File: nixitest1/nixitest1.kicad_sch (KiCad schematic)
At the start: 32 parts, among them J1 MSYS, Q1 60V 3A, Q10 HVN, Q11 HVN, Q12 HVN, Q13 HVN, Q2 HVN, Q3 HVN, Q4 HVN, Q5 HVN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

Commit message: Update schematic and design.
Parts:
- added J5, J6: ~, rawpad22:rawpad22, symbol Connector_Generic:Conn_01x01
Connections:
- net PGM: now also J5.1 (Pin_1); no longer J4.1 (Pin_1)
- net URX: now also J4.1 (Pin_1)
- net UTX: now also J6.1 (Pin_1)
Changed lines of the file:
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@@
+    )
+  )
+  (global_label "UTX" (shape input) (at 132.08 177.8 270) (fields_autoplaced)
+    (effects (font (size 1.27 1.27)) (justify right))
+    (property "Intersheet References" "${INTERSHEET_REFS}" (id 0) (at 132.0006 183.7207 90)
+      (effects (font (size 1.27 1.27)) (justify right) hide)
     )
   )
@@
     )
   )
-  (global_label "PGM" (shape input) (at 166.37 165.1 270) (fields_autoplaced)
-    (effects (font (size 1.27 1.27)) (justify right))
-    (property "Intersheet References" "${INTERSHEET_REFS}" (id 0) (at 166.4494 171.5045 90)
+  (global_label "PGM" (shape input) (at 129.54 177.8 270) (fields_autoplaced)
+    (effects (font (size 1.27 1.27)) (justify right))
+    (property "Intersheet References" "${INTERSHEET_REFS}" (id 0) (at 129.6194 184.2045 90)
+      (effects (font (size 1.27 1.27)) (justify right) hide)
+    )
+  )
+  (global_label "URX" (shape input) (at 124.46 177.8 270) (fields_autoplaced)
+    (effects (font (size 1.27 1.27)) (justify right))
+    (property "Intersheet References" "${INTERSHEET_REFS}" (id 0) (at 124.3806 184.0231 90)
       (effects (font (size 1.27 1.27)) (justify right) hide)
     )
@@
     )
   )
+  (symbol (lib_id "Connector_Generic:Conn_01x01") (at 132.08 172.72 90) (unit 1)
+    (in_bom yes) (on_board yes)
+    (property "Reference" "J6" (id 0) (at 134.62 171.4499 90)
+      (effects (font (size 1.27 1.27)) (justify right) hide)
+    )
+    (property "Value" "~" (id 1) (at 116.84 173.9899 90)
+      (effects (font (size 1.27 1.27)) (justify right))
+    )
+    (property "Footprint" "rawpad22:rawpad22" (id 2) (at 132.08 172.72 0)
+      (effects (font (size 1.27 1.27)) hide)
+    )
+    (property "Datasheet" "~" (id 3) (at 132.08 172.72 0)
+      (effects (font (size 1.27 1.27)) hide)
+    )
+    (pin "1")
+  )
   (symbol (lib_id "power:GND") (at 256.54 114.3 0) (unit 1)
     (in_bom yes) (on_board yes) (fields_autoplaced)
@@
     (pin "1")
   )
-  (symbol (lib_id "Connector_Generic:Conn_01x01") (at 161.29 160.02 90) (unit 1)
-    (in_bom yes) (on_board yes) (fields_autoplaced)
-    (property "Reference" "J2" (id 0) (at 163.83 158.7499 90)
-      (effects (font (size 1.27 1.27)) (justify right) hide)
-    )
-    (property "Value" "~" (id 1) (at 163.83 161.2899 90)
+  (symbol (lib_id "Connector_Generic:Conn_01x01") (at 121.92 172.72 90) (unit 1)
+    (in_bom yes) (on_board yes)
+    (property "Reference" "J2" (id 0) (at 124.46 171.4499 90)
+      (effects (font (size 1.27 1.27)) (justify right) hide)
+    )
+    (property "Value" "~" (id 1) (at 129.54 173.9899 90)
       (effects (font (size 1.27 1.27)) (justify right))
     )
-    (property "Footprint" "rawpad22:rawpad22" (id 2) (at 161.29 160.02 0)
-      (effects (font (size 1.27 1.27)) hide)
-    )
-    (property "Datasheet" "~" (id 3) (at 161.29 160.02 0)
+    (property "Footprint" "rawpad22:rawpad22" (id 2) (at 121.92 172.72 0)
+      (effects (font (size 1.27 1.27)) hide)
+    )
+    (property "Datasheet" "~" (id 3) (at 121.92 172.72 0)
       (effects (font (size 1.27 1.27)) hide)
     )
@@
     (pin "1")
   )
-  (symbol (lib_id "Connector_Generic:Conn_01x01") (at 166.37 160.02 90) (unit 1)
-    (in_bom yes) (on_board yes) (fields_autoplaced)
-    (property "Reference" "J4" (id 0) (at 168.91 158.7499 90)
-      (effects (font (size 1.27 1.27)) (justify right) hide)
-    )
-    (property "Value" "~" (id 1) (at 168.91 161.2899 90)
+  (symbol (lib_id "Connector_Generic:Conn_01x01") (at 124.46 172.72 90) (unit 1)
+    (in_bom yes) (on_board yes) (fields_autoplaced)
+    (property "Reference" "J4" (id 0) (at 127 171.4499 90)
+      (effects (font (size 1.27 1.27)) (justify right) hide)
+    )
+    (property "Value" "~" (id 1) (at 127 173.9899 90)
       (effects (font (size 1.27 1.27)) (justify right))
     )
-    (property "Footprint" "rawpad22:rawpad22" (id 2) (at 166.37 160.02 0)
-      (effects (font (size 1.27 1.27)) hide)
-    )
-    (property "Datasheet" "~" (id 3) (at 166.37 160.02 0)
+    (property "Footprint" "rawpad22:rawpad22" (id 2) (at 124.46 172.72 0)
+      (effects (font (size 1.27 1.27)) hide)
+    )
+    (property "Datasheet" "~" (id 3) (at 124.46 172.72 0)
       (effects (font (size 1.27 1.27)) hide)
     )
@@
     (pin "1")
   )
-  (symbol (lib_id "power:+5V") (at 163.83 165.1 180) (unit 1)
-    (in_bom yes) (on_board yes)
-    (property "Reference" "#PWR0131" (id 0) (at 163.83 161.29 0)
-      (effects (font (size 1.27 1.27)) hide)
-    )
-    (property "Value" "+5V" (id 1) (at 163.83 172.72 90)
+  (symbol (lib_id "power:+5V") (at 127 177.8 180) (unit 1)
+    (in_bom yes) (on_board yes)
+    (property "Reference" "#PWR0131" (id 0) (at 127 173.99 0)
+      (effects (font (size 1.27 1.27)) hide)
+    )
+    (property "Value" "+5V" (id 1) (at 127 185.42 90)
       (effects (font (size 1.27 1.27)) (justify right))
     )
-    (property "Footprint" "" (id 2) (at 163.83 165.1 0)
-      (effects (font (size 1.27 1.27)) hide)
-    )
-    (property "Datasheet" "" (id 3) (at 163.83 165.1 0)
-      (effects (font (size 1.27 1.27)) hide)
-    )
-    (pin "1")
-  )
-  (symbol (lib_id "power:GND") (at 161.29 165.1 0) (unit 1)
-    (in_bom yes) (on_board yes)
-    (property "Reference" "#PWR0134" (id 0) (at 161.29 171.45 0)
-      (effects (font (size 1.27 1.27)) hide)
-    )
-    (property "Value" "GND" (id 1) (at 161.29 172.72 90)
-      (effects (font (size 1.27 1.27)) (justify left))
-    )
-    (property "Footprint" "" (id 2) (at 161.29 165.1 0)
-      (effects (font (size 1.27 1.27)) hide)
-    )
-    (property "Datasheet" "" (id 3) (at 161.29 165.1 0)
+    (property "Footprint" "" (id 2) (at 127 177.8 0)
+      (effects (font (size 1.27 1.27)) hide)
+    )
+    (property "Datasheet" "" (id 3) (at 127 177.8 0)
+      (effects (font (size 1.27 1.27)) hide)
+    )
+    (pin "1")
+  )
+  (symbol (lib_id "power:GND") (at 121.92 177.8 0) (unit 1)
+    (in_bom yes) (on_board yes)
+    (property "Reference" "#PWR0134" (id 0) (at 121.92 184.15 0)
+      (effects (font (size 1.27 1.27)) hide)
+    )
+    (property "Value" "GND" (id 1) (at 121.92 185.42 90)
+      (effects (font (size 1.27 1.27)) (justify left))
+    )
+    (property "Footprint" "" (id 2) (at 121.92 177.8 0)
+      (effects (font (size 1.27 1.27)) hide)
+    )
+    (property "Datasheet" "" (id 3) (at 121.92 177.8 0)
       (effects (font (size 1.27 1.27)) hide)
     )
@@
     (pin "3")
   )
-  (symbol (lib_id "Connector_Generic:Conn_01x01") (at 163.83 160.02 90) (unit 1)
-    (in_bom yes) (on_board yes) (fields_autoplaced)
-    (property "Reference" "J3" (id 0) (at 166.37 158.7499 90)
-      (effects (font (size 1.27 1.27)) (justify right) hide)
-    )
-    (property "Value" "~" (id 1) (at 166.37 161.2899 90)
+  (symbol (lib_id "Connector_Generic:Conn_01x01") (at 127 172.72 90) (unit 1)
+    (in_bom yes) (on_board yes)
+    (property "Reference" "J3" (id 0) (at 129.54 171.4499 90)
+      (effects (font (size 1.27 1.27)) (justify right) hide)
+    )
+    (property "Value" "~" (id 1) (at 130.81 173.9899 90)
       (effects (font (size 1.27 1.27)) (justify right))
     )
-    (property "Footprint" "rawpad22:rawpad22" (id 2) (at 163.83 160.02 0)
-      (effects (font (size 1.27 1.27)) hide)
-    )
-    (property "Datasheet" "~" (id 3) (at 163.83 160.02 0)
+    (property "Footprint" "rawpad22:rawpad22" (id 2) (at 127 172.72 0)
+      (effects (font (size 1.27 1.27)) hide)
+    )
+    (property "Datasheet" "~" (id 3) (at 127 172.72 0)
       (effects (font (size 1.27 1.27)) hide)
     )
@@
     (pin "3")
     (pin "4")
+  )
+  (symbol (lib_id "Connector_Generic:Conn_01x01") (at 129.54 172.72 90) (unit 1)
+    (in_bom yes) (on_board yes) (fields_autoplaced)
+    (property "Reference" "J5" (id 0) (at 132.08 171.4499 90)
+      (effects (font (size 1.27 1.27)) (justify right) hide)
+    )
+    (property "Value" "~" (id 1) (at 132.08 173.9899 90)
+      (effects (font (size 1.27 1.27)) (justify right))
+    )
+    (property "Footprint" "rawpad22:rawpad22" (id 2) (at 129.54 172.72 0)
+      (effects (font (size 1.27 1.27)) hide)
+    )
+    (property "Datasheet" "~" (id 3) (at 129.54 172.72 0)
+      (effects (font (size 1.27 1.27)) hide)
+    )
+    (pin "1")
   )
   (symbol (lib_id "Device:R") (at 52.07 123.19 180) (unit 1)
@@
       (reference "J4") (unit 1) (value "~") (footprint "rawpad22:rawpad22")
     )
+    (path "/f434e5f4-d301-4161-a4e0-864b47e33319"
+      (reference "J5") (unit 1) (value "~") (footprint "rawpad22:rawpad22")
+    )
+    (path "/01b473f5-b618-4401-b7ef-ab926d8af868"
+      (reference "J6") (unit 1) (value "~") (footprint "rawpad22:rawpad22")
+    )
     (path "/6391ffee-64ab-4dc8-a08c-807c55cf112f"

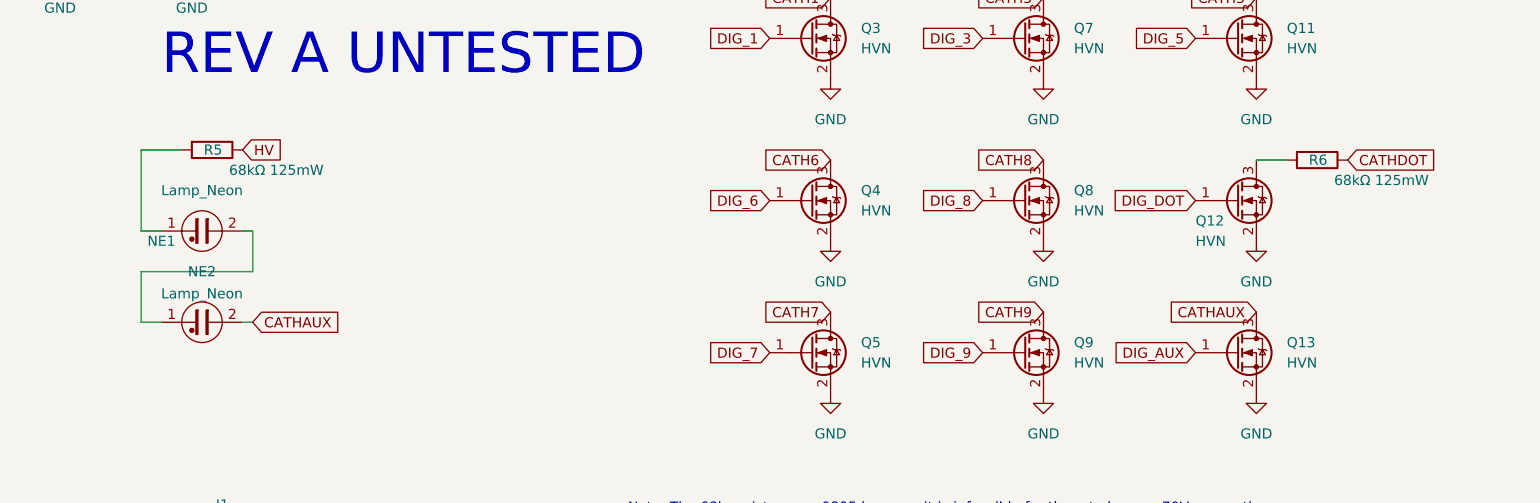
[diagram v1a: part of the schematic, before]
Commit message: Adjust resistors to reduce max power to neons and period.
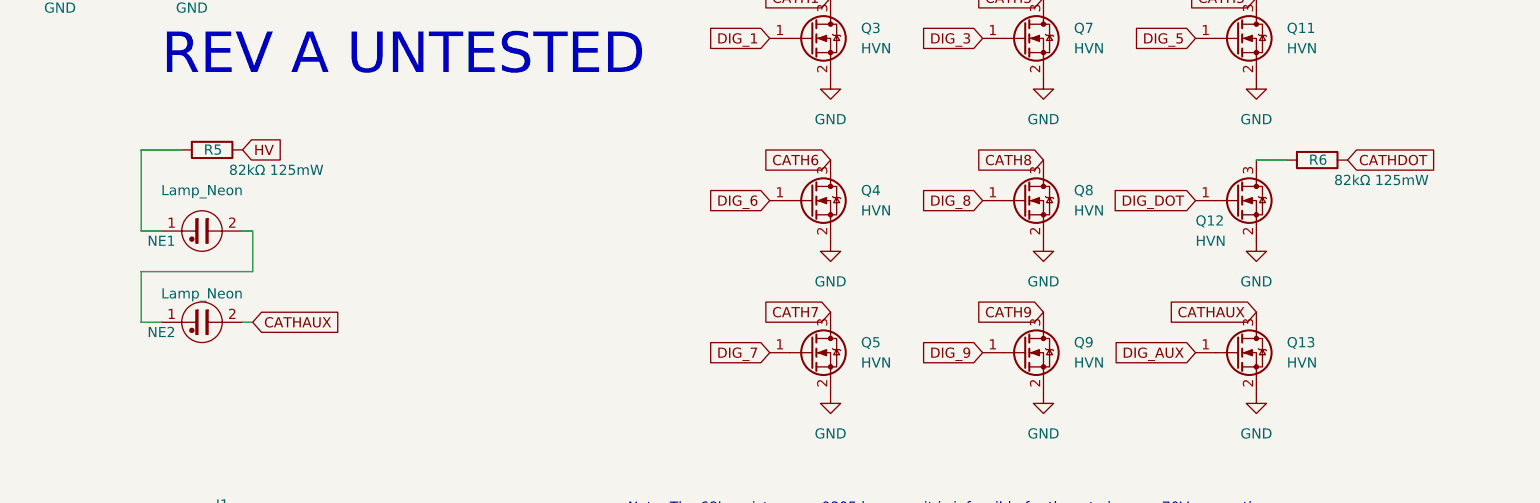
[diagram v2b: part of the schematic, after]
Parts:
- R5, R6: value 68kΩ 125mW -> 82kΩ 125mW; LCSC C114548 -> C136904
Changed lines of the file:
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@@
   (symbol (lib_id "Device:Lamp_Neon") (at 124.46 124.46 270) (unit 1)
     (in_bom yes) (on_board yes)
-    (property "Reference" "NE2" (id 0) (at 124.46 118.11 90))
+    (property "Reference" "NE2" (id 0) (at 119.38 125.73 90))
     (property "Value" "Lamp_Neon" (id 1) (at 124.46 120.8841 90))
     (property "Footprint" "neonglow:neonglow" (id 2) (at 127 124.46 90)
@@
       (effects (font (size 1.27 1.27)) (justify right))
     )
-    (property "Value" "68kΩ 125mW" (id 1) (at 278.13 106.68 90)
+    (property "Value" "82kΩ 125mW" (id 1) (at 278.13 106.68 90)
       (effects (font (size 1.27 1.27)) (justify right))
     )
@@
       (effects (font (size 1.27 1.27)) hide)
     )
-    (property "LCSC" "C114548" (id 4) (at 264.16 104.14 90)
+    (property "LCSC" "C136904" (id 4) (at 264.16 104.14 90)
       (effects (font (size 1.27 1.27)) hide)
     )
@@
     (pin "3")
   )
-  (symbol (lib_id "Device:R") (at 125.73 102.87 270) (unit 1)
-    (in_bom yes) (on_board yes)
-    (property "Reference" "R5" (id 0) (at 127 102.87 90)
-      (effects (font (size 1.27 1.27)) (justify right))
-    )
-    (property "Value" "68kΩ 125mW" (id 1) (at 139.7 105.41 90)
-      (effects (font (size 1.27 1.27)) (justify right))
-    )
-    (property "Footprint" "Resistor_SMD:R_0805_2012Metric" (id 2) (at 125.73 101.092 90)
-      (effects (font (size 1.27 1.27)) hide)
-    )
-    (property "Datasheet" "~" (id 3) (at 125.73 102.87 0)
-      (effects (font (size 1.27 1.27)) hide)
-    )
-    (property "LCSC" "C114548" (id 4) (at 125.73 102.87 90)
-      (effects (font (size 1.27 1.27)) hide)
-    )
-    (pin "1")
-    (pin "2")
-  )
   (symbol (lib_id "power:GND") (at 133.35 163.83 90) (unit 1)
     (in_bom yes) (on_board yes)
@@
     )
     (pin "1")
+  )
+  (symbol (lib_id "Device:R") (at 125.73 102.87 270) (unit 1)
+    (in_bom yes) (on_board yes)
+    (property "Reference" "R5" (id 0) (at 127 102.87 90)
+      (effects (font (size 1.27 1.27)) (justify right))
+    )
+    (property "Value" "82kΩ 125mW" (id 1) (at 139.7 105.41 90)
+      (effects (font (size 1.27 1.27)) (justify right))
+    )
+    (property "Footprint" "Resistor_SMD:R_0805_2012Metric" (id 2) (at 125.73 101.092 90)
+      (effects (font (size 1.27 1.27)) hide)
+    )
+    (property "Datasheet" "~" (id 3) (at 125.73 102.87 0)
+      (effects (font (size 1.27 1.27)) hide)
+    )
+    (property "LCSC" "C136904" (id 4) (at 125.73 102.87 90)
+      (effects (font (size 1.27 1.27)) hide)
+    )
+    (pin "1")
+    (pin "2")
   )
   (symbol (lib_id "Device:R") (at 52.07 123.19 180) (unit 1)
@@
       (reference "R4") (unit 1) (value "15kΩ 1206 1% 250mW") (footprint "Resistor_SMD:R_1206_3216Metric")
     )
-    (path "/7bd8b117-de82-4f65-8169-3809d7aafa7c"
-      (reference "R5") (unit 1) (value "68kΩ 125mW") (footprint "Resistor_SMD:R_0805_2012Metric")
+    (path "/f9c6bb79-fcee-4b31-8d57-04ead19a0cd8"
+      (reference "R5") (unit 1) (value "82kΩ 125mW") (footprint "Resistor_SMD:R_0805_2012Metric")
     )
     (path "/4960ffe3-3f54-4853-a1a0-f864a90e8c9e"
-      (reference "R6") (unit 1) (value "68kΩ 125mW") (footprint "Resistor_SMD:R_0805_2012Metric")
+      (reference "R6") (unit 1) (value "82kΩ 125mW") (footprint "Resistor_SMD:R_0805_2012Metric")
     )
     (path "/f3fcf9c2-f40b-4ecf-9467-7bb68ac2c8f3"

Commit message: Update to rev B.
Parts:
- C1: footprint Capacitor_SMD:C_1206_3216Metric -> Capacitor_SMD:C_1210_3225Metric; LCSC C377089 -> C326671
- C3: value 100n -> 220nF; LCSC C1525 -> C16772
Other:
- note added: "Changes in RevA * Probably remove HVIMON >> DEFINITELY * Include pull-down on HVCTL >> DEFINITELY. * Monitor ripple on HVP (NOT AN ISSUE) * Switch resistors to 15k * Transformer should have both rails tied to 5V * Aux resistor independent of anode resistor. * Aux Neons in series. * Shrunk bulk capacitor to 1206 * Feedback resistor to 1206 Rev A Discussion Mod HW per Ivan. * Shrink binding post ho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"
- note removed: "Changes in RevA * Probably remove HVIMON >> DEFINITELY * Include pull-down on HVCTL >> DEFINITELY. * Monitor ripple on HVP (NOT AN ISSUE) * Switch resistors to 15k * Transformer should have both rails tied to 5V * Aux resistor independent of anode resistor. * Aux Neons in series. * Shrunk bulk capacitor to 1206 * Feedback resistor to 1206 TODO: Mod HW per Ivan. * Shrink binding post holes. * Mark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"
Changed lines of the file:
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@@
     (effects (font (size 1.27 1.27)) (justify left bottom))
   )
-  (text "Changes in RevA\n * Probably remove HVIMON >> DEFINITELY\n * Include pull-down on HVCTL  >> DEFINITELY.\n * Monitor ripple on HVP  (NOT AN ISSUE)\n * Switch resistors to 15k\n * Transformer should have both rails tied to 5V \n * Aux resistor independent of anode resistor.\n * Aux Neons in series.\n * Shrunk bulk capacitor to 1206\n * Feedback resistor to 1206\nTODO:\nMod HW per Ivan.\n * Shrink binding post holes.\n * Mark off which pin on header is PGM\n * Reduce power to comma\n * Flip orientation of tube?"
+  (text "Changes in RevA\n * Probably remove HVIMON >> DEFINITELY\n * Include pull-down on HVCTL  >> DEFINITELY.\n * Monitor ripple on HVP  (NOT AN ISSUE)\n * Switch resistors to 15k\n * Transformer should have both rails tied to 5V \n * Aux resistor independent of anode resistor.\n * Aux Neons in series.\n * Shrunk bulk capacitor to 1206\n * Feedback resistor to 1206\nRev A Discussion\nMod HW per Ivan.\n * Shrink binding post holes.\n * Mark off which pin on header is PGM\n * Reduce power to comma\n * Flip orientation of tube?\nRev B:\n * Switch back to 1210 main cap.\n > C377089 to C326671"
     (at 22.86 173.99 0)
     (effects (font (size 1.27 1.27)) (justify left bottom))
@@
       (effects (font (size 1.27 1.27)) (justify left))
     )
-    (property "Footprint" "Capacitor_SMD:C_1206_3216Metric" (id 2) (at 63.1952 121.92 0)
+    (property "Footprint" "Capacitor_SMD:C_1210_3225Metric" (id 2) (at 63.1952 121.92 0)
       (effects (font (size 1.27 1.27)) hide)
     )
@@
       (effects (font (size 1.27 1.27)) hide)
     )
-    (property "LCSC" "C377089" (id 4) (at 62.23 118.11 0)
+    (property "LCSC" "C326671" (id 4) (at 62.23 118.11 0)
       (effects (font (size 1.27 1.27)) hide)
     )
@@
       (effects (font (size 1.27 1.27)) (justify left))
     )
-    (property "Value" "100n" (id 1) (at 110.49 77.4699 0)
+    (property "Value" "220nF" (id 1) (at 110.49 77.4699 0)
       (effects (font (size 1.27 1.27)) (justify left))
     )
@@
       (effects (font (size 1.27 1.27)) hide)
     )
-    (property "LCSC" "C1525" (id 4) (at 106.68 76.2 0)
+    (property "LCSC" "C16772" (id 4) (at 106.68 76.2 0)
       (effects (font (size 1.27 1.27)) hide)
     )
@@
     )
     (path "/2482b284-20c0-4ecb-b135-d475161041a6"
-      (reference "C1") (unit 1) (value "220nF 250V") (footprint "Capacitor_SMD:C_1206_3216Metric")
+      (reference "C1") (unit 1) (value "220nF 250V") (footprint "Capacitor_SMD:C_1210_3225Metric")
     )
     (path "/ce857e03-9713-423a-aa86-5e9cf13252ba"
@@
     )
     (path "/c0e4e818-7a15-45d3-98f1-752f12bf617a"
-      (reference "C3") (unit 1) (value "100n") (footprint "Capacitor_SMD:C_0402_1005Metric")
+      (reference "C3") (unit 1) (value "220nF") (footprint "Capacitor_SMD:C_0402_1005Metric")
     )
     (path "/cf8069de-fc54-48f6-88fa-856cb03f39a0"

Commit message: Update schematic etc for rev b.
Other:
- note added: "REV B UNTESTED"
- note removed: "REV A UNTESTED"
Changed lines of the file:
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@@
     (effects (font (size 1.27 1.27)) (justify left bottom))
   )
-  (text "REV A UNTESTED" (at 119.38 93.98 0)
+  (text "REV B UNTESTED" (at 119.38 93.98 0)
     (effects (font (size 5.08 5.08)) (justify left bottom))
   )
